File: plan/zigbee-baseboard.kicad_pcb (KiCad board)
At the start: 4 copper layers, 15.3 x 20.6 mm, 55 parts, among them J1 Debug_SWD_Pogo_2x3, J2 EFR32MG24_Core_Expansion_L12, SW1 EVPBB2A9B000, U1 EFR32MG24B020F1536IM48-B, Y1 XTL501250-S315-038

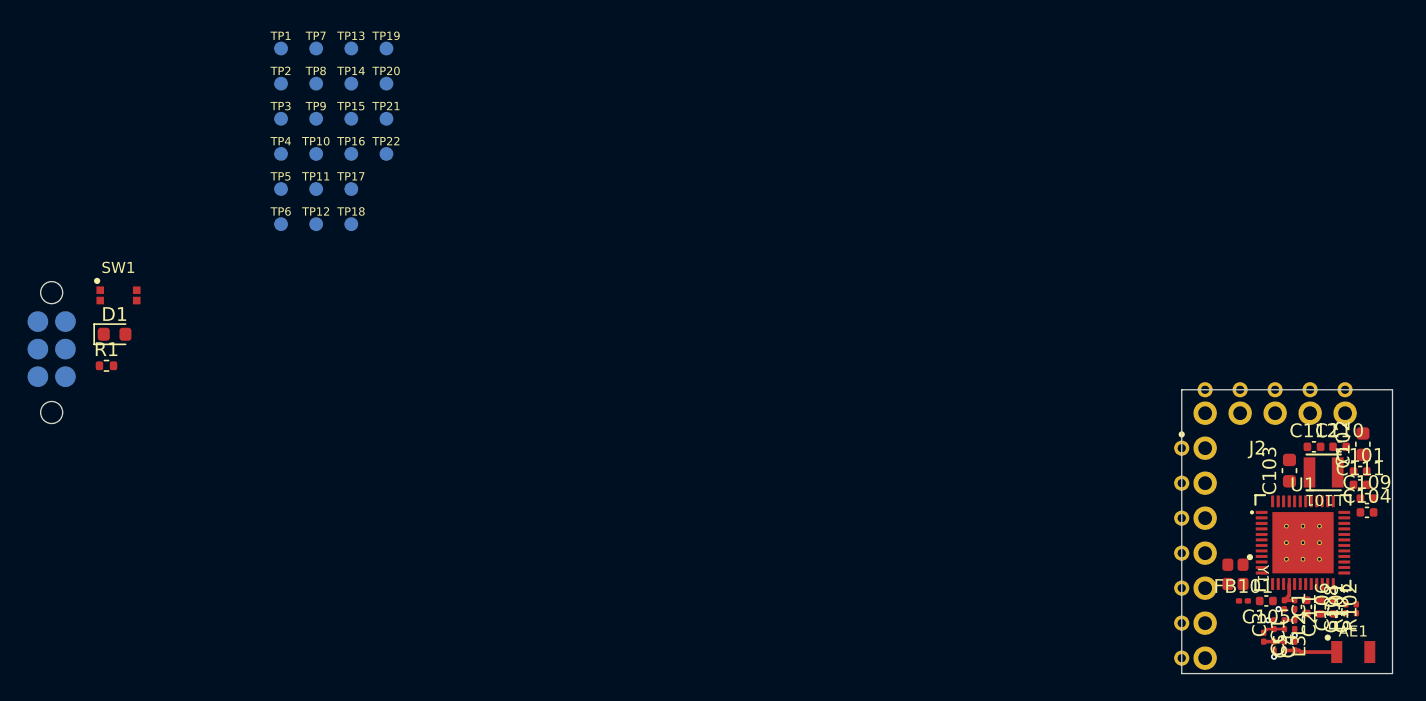
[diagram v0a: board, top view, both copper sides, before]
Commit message: Adapt and place programming/debug pad
- Remove NPTH holes because they require too much space
- Place pad on board bottom side
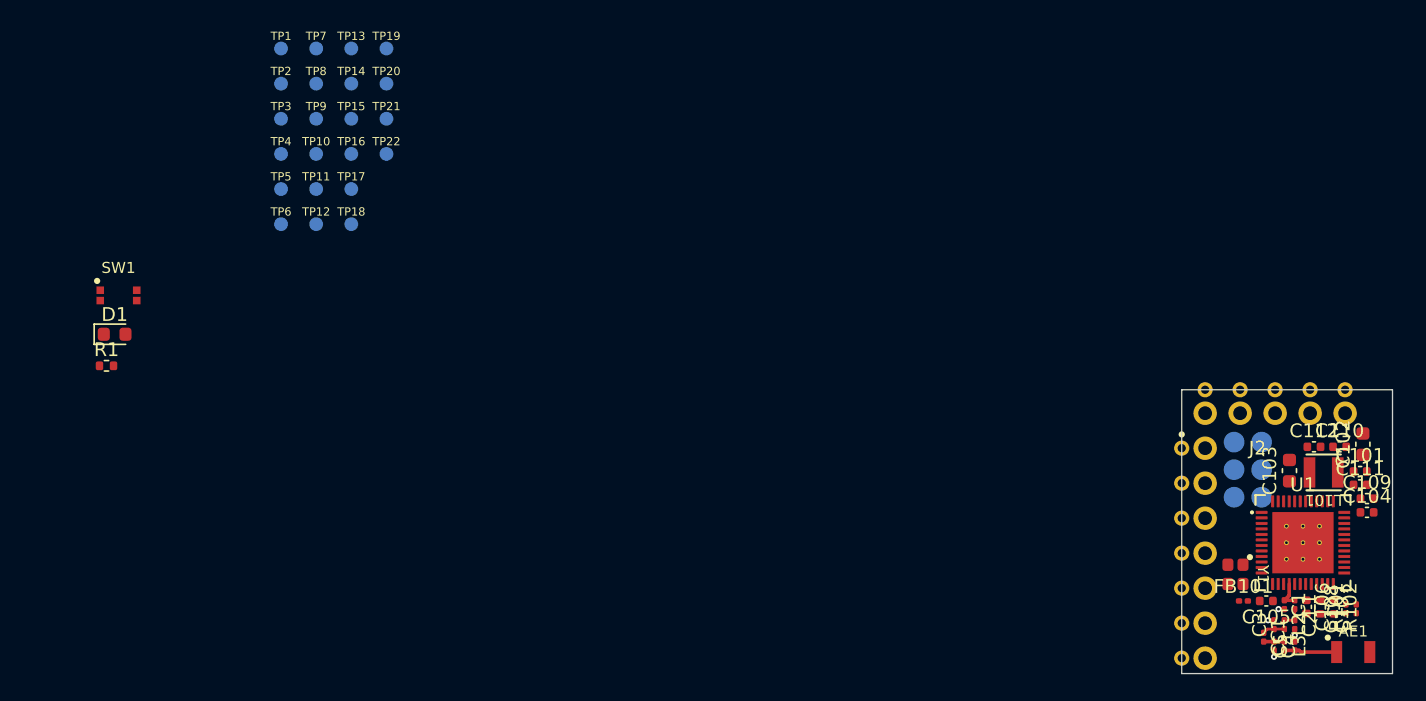
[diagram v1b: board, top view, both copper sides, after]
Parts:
- J1: value Debug_SWD_Pogo_2x3 -> Debug_SWD_Pogo_2x3_P2.00mm
- moved J1 87.3 mm to (139.0, 88.2), turned to 180 degrees
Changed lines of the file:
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@@
 		(sheetname "/Expansion/")
 		(sheetfile "Expansion.kicad_sch")
+		(units
+			(unit
+				(name "A")
+				(pins "1" "2" "3" "4" "5" "6" "7" "8" "9" "10" "11" "12")
+			)
+		)
 		(attr smd)
 		(duplicate_pad_numbers_are_jumpers no)
@@
 	)
 	(footprint "Smarthome:Debug_SWD_Pogo_2x3_P2.00mm"
+		(locked yes)
 		(layer "F.Cu")
-		(at 52.175 79.45)
+		(at 139 88.2 180)
+		(descr "6-pin 2x3 SWD pogo-pad interface, 2.00 mm pitch, bottom-side SMD contact pads, without alignment holes")
+		(tags "SWD debug pogo programming 2x3 2.00mm bottom")
 		(property "Reference" "J1"
-			(at 0 -5.8 0)
+			(at 0 -5.8 180)
 			(unlocked yes)
 			(layer "B.SilkS")
@@
 			)
 		)
-		(property "Value" "Debug_SWD_Pogo_2x3"
-			(at 0 7.5 0)
+		(property "Value" "Debug_SWD_Pogo_2x3_P2.00mm"
+			(at 0 7.5 180)
 			(unlocked yes)
 			(layer "F.Fab")
@@
 		)
 		(property "Datasheet" ""
-			(at 0 0 0)
-			(unlocked yes)
-			(layer "F.Fab")
-			(hide yes)
-			(effects
-				(font
-					(size 1 1)
-					(thickness 0.15)
-				)
-			)
-		)
-		(property "Description" "6-pin SWD programming interface with 2x3 pogo pads and two asymmetric NPTH alignment holes"
-			(at 0 0 0)
+			(at 0 0 180)
+			(unlocked yes)
+			(layer "F.Fab")
+			(hide yes)
+			(effects
+				(font
+					(size 1 1)
+					(thickness 0.15)
+				)
+			)
+		)
+		(property "Description" "6-pin SWD pogo programming interface, 2x3, 2.00 mm pitch, without alignment holes"
+			(at 0 0 180)
 			(unlocked yes)
 			(layer "F.Fab")
@@
 		(sheetname "/UserDebug/")
 		(sheetfile "UserDebug.kicad_sch")
-		(units
-			(unit
-				(name "A")
-				(pins "1" "2" "3" "4" "5" "6")
-			)
-		)
 		(attr smd)
 		(duplicate_pad_numbers_are_jumpers no)
@@
 		)
 		(fp_rect
-			(start -2 -5.15)
-			(end 2 5.65)
+			(start -2 -3)
+			(end 2 3)
 			(stroke
 				(width 0.05)
@@
 		)
 		(fp_text user "${REFERENCE}"
-			(at 0 6.3 0)
+			(at 0 6.3 180)
 			(unlocked yes)
 			(layer "B.Fab")
@@
 			)
 		)
-		(pad "" np_thru_hole circle
-			(at 0 -4.1)
-			(size 1.6 1.6)
-			(drill 1.6)
-			(layers "*.Cu" "*.Mask")
-		)
-		(pad "" np_thru_hole circle
-			(at 0 4.6)
-			(size 1.6 1.6)
-			(drill 1.6)
-			(layers "*.Cu" "*.Mask")
-		)
 		(pad "1" smd circle
-			(at -1 -2)
+			(at -1 -2 180)
 			(size 1.5 1.5)
 			(layers "B.Cu" "B.Mask")
@@
 		)
 		(pad "2" smd circle
-			(at 1 -2)
+			(at 1 -2 180)
 			(size 1.5 1.5)
 			(layers "B.Cu" "B.Mask")
@@
 		)
 		(pad "3" smd circle
-			(at -1 0)
+			(at -1 0 180)
 			(size 1.5 1.5)
 			(layers "B.Cu" "B.Mask")
@@
 		)
 		(pad "4" smd circle
-			(at 1 0)
+			(at 1 0 180)
 			(size 1.5 1.5)
 			(layers "B.Cu" "B.Mask")
@@
 		)
 		(pad "5" smd circle
-			(at -1 2)
+			(at -1 2 180)
 			(size 1.5 1.5)
 			(layers "B.Cu" "B.Mask")
@@
 		)
 		(pad "6" smd circle
-			(at 1 2)
+			(at 1 2 180)
 			(size 1.5 1.5)
 			(layers "B.Cu" "B.Mask")

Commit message: Place pairing-button
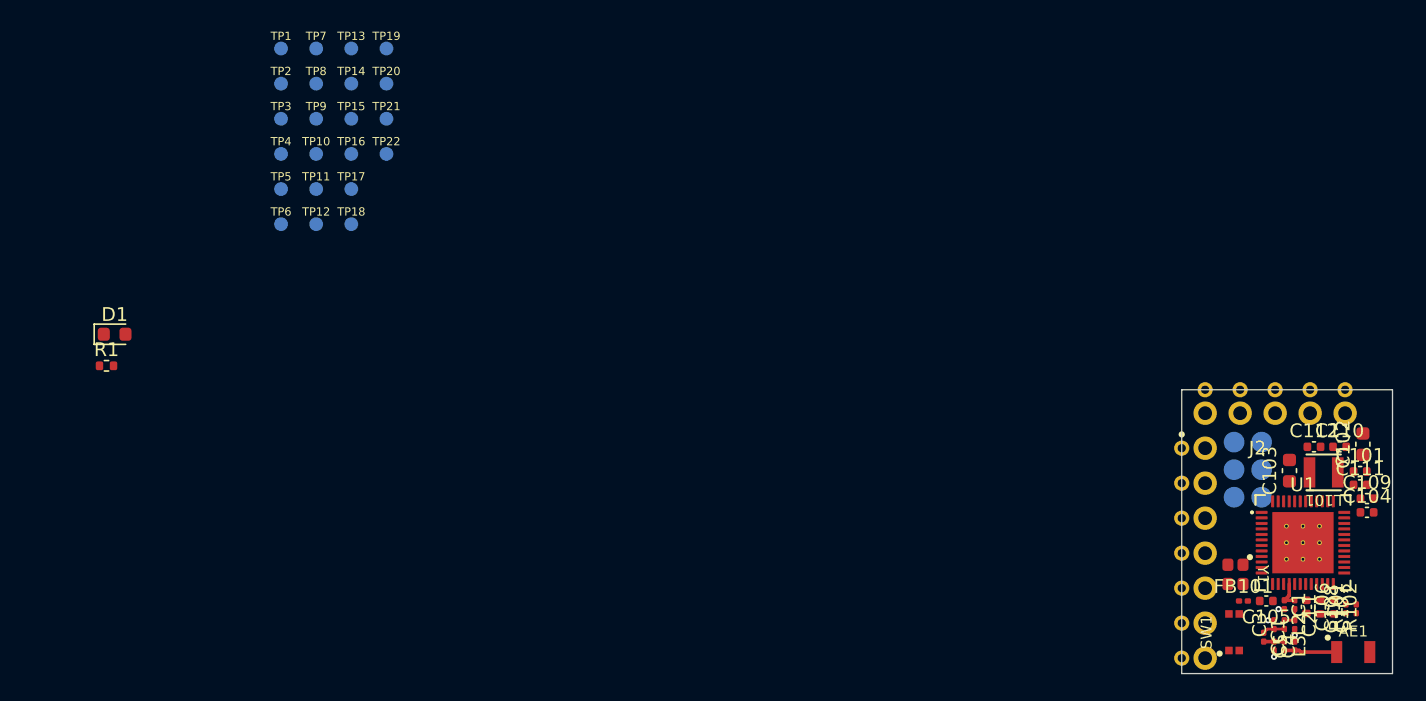
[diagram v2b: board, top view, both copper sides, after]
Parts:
- moved SW1 84.6 mm to (138.0, 100.0), turned to 90 degrees
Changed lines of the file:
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@@
 	)
 	(footprint "Smarthome:Button_Panasonic_EVPBB_2.6x1.6mm"
+		(locked yes)
 		(layer "F.Cu")
-		(at 57.025 75.55)
+		(at 138 100 90)
 		(descr "Panasonic EVP-BB series SMD light touch switch, 2.6 x 1.6 mm, top push, 4 pads")
 		(tags "Panasonic EVPBB EVP-BB tactile switch button 2.6x1.6 SMD")
 		(property "Reference" "SW1"
-			(at 0 -2 0)
+			(at 0 -2 90)
 			(unlocked yes)
 			(layer "F.SilkS")
@@
 		)
 		(property "Value" "EVPBB2A9B000"
-			(at 0 2 0)
+			(at 0 2 90)
 			(unlocked yes)
 			(layer "F.Fab")
@@
 		)
 		(property "Datasheet" "https://industrial.panasonic.com/cdbs/www-data/pdf/ATK0000/ATK0000C362.pdf"
-			(at 0 0 0)
+			(at 0 0 90)
 			(unlocked yes)
 			(layer "F.Fab")
@@
 		)
 		(property "Description" "Panasonic EVPBB2A9B000, SMD light touch switch, SPST-NO, top push, 2.6 x 1.6 x 0.53 mm, 1.6 N"
-			(at 0 0 0)
+			(at 0 0 90)
 			(unlocked yes)
 			(layer "F.Fab")
@@
 		)
 		(fp_line
+			(start 1.3 -0.8)
+			(end -1 -0.8)
+			(stroke
+				(width 0.1)
+				(type default)
+			)
+			(layer "F.Fab")
+		)
+		(fp_line
 			(start -1.3 -0.5)
 			(end -1 -0.8)
+			(stroke
+				(width 0.1)
+				(type default)
+			)
+			(layer "F.Fab")
+		)
+		(fp_line
+			(start 1.3 0.8)
+			(end 1.3 -0.8)
 			(stroke
 				(width 0.1)
@@
 			(layer "F.Fab")
 		)
-		(fp_line
-			(start 1.3 -0.8)
-			(end -1 -0.8)
-			(stroke
-				(width 0.1)
-				(type default)
-			)
-			(layer "F.Fab")
-		)
-		(fp_line
-			(start 1.3 0.8)
-			(end 1.3 -0.8)
-			(stroke
-				(width 0.1)
-				(type default)
-			)
-			(layer "F.Fab")
-		)
 		(fp_text user "${REFERENCE}"
-			(at 0 0 0)
+			(at 0 0 90)
 			(unlocked yes)
 			(layer "F.Fab")
@@
 		)
 		(pad "1" smd rect
-			(at -1.325 -0.375)
+			(at -1.325 -0.375 90)
 			(size 0.55 0.55)
 			(layers "F.Cu" "F.Mask" "F.Paste")
@@
 		)
 		(pad "1" smd rect
-			(at -1.325 0.375)
+			(at -1.325 0.375 90)
 			(size 0.55 0.55)
 			(layers "F.Cu" "F.Mask" "F.Paste")
@@
 		)
 		(pad "2" smd rect
-			(at 1.325 -0.375)
+			(at 1.325 -0.375 90)
 			(size 0.55 0.55)
 			(layers "F.Cu" "F.Mask" "F.Paste")
@@
 		)
 		(pad "2" smd rect
-			(at 1.325 0.375)
+			(at 1.325 0.375 90)
 			(size 0.55 0.55)
 			(layers "F.Cu" "F.Mask" "F.Paste")

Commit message: Place status LED
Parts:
- moved D1 83.0 mm to (138.4, 93.0), turned to -90 degrees
- moved R1 82.0 mm to (137.2, 93.0), turned to -90 degrees
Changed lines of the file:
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@@
 	)
 	(footprint "LED_SMD:LED_0603_1608Metric"
+		(locked yes)
 		(layer "F.Cu")
-		(at 56.745 78.37)
+		(at 138.4 93 -90)
 		(descr "LED SMD 0603 (1608 Metric), square (rectangular) end terminal, IPC-7351 nominal, (Body size source: http://www.tortai-tech.com/upload/download/2011102023233369053.pdf)")
 		(tags "LED")
 		(property "Reference" "D1"
-			(at 0 -1.43 0)
+			(at 0 -1.43 90)
 			(layer "F.SilkS")
 			(effects
@@
 		)
 		(property "Value" "APT1608LZGCK"
-			(at 0 1.43 0)
+			(at 0 1.43 90)
 			(layer "F.Fab")
 			(effects
@@
 		)
 		(property "Datasheet" ""
-			(at 0 0 0)
+			(at 0 0 90)
 			(layer "F.Fab")
 			(hide yes)
@@
 		)
 		(property "Description" "Light emitting diode"
-			(at 0 0 0)
+			(at 0 0 90)
 			(layer "F.Fab")
 			(hide yes)
@@
 		)
 		(property "KiLib_Generator" "SMD_2terminal_chip_molded"
-			(at 0 0 0)
+			(at 0 0 90)
 			(layer "F.SilkS")
 			(hide yes)
@@
 		)
 		(property "Sim.Pins" "1=K 2=A"
-			(at 0 0 0)
+			(at 0 0 270)
 			(unlocked yes)
 			(layer "F.Fab")
@@
 		)
 		(property "Manufacturer" "Kingbright"
-			(at 0 0 0)
+			(at 0 0 270)
 			(unlocked yes)
 			(layer "F.Fab")
@@
 		)
 		(property "Color" "green"
-			(at 0 0 0)
+			(at 0 0 270)
 			(unlocked yes)
 			(layer "F.Fab")
@@
 		)
 		(property "Package" "0603 / 1608 metric"
-			(at 0 0 0)
+			(at 0 0 270)
 			(unlocked yes)
 			(layer "F.Fab")
@@
 		(duplicate_pad_numbers_are_jumpers no)
 		(fp_line
+			(start -1.485 0.735)
+			(end 0.8 0.735)
+			(stroke
+				(width 0.12)
+				(type solid)
+			)
+			(layer "F.SilkS")
+		)
+		(fp_line
 			(start -1.485 -0.735)
 			(end -1.485 0.735)
-			(stroke
-				(width 0.12)
-				(type solid)
-			)
-			(layer "F.SilkS")
-		)
-		(fp_line
-			(start -1.485 0.735)
-			(end 0.8 0.735)
 			(stroke
 				(width 0.12)
@@
 		)
 		(fp_line
+			(start -0.8 0.4)
+			(end 0.8 0.4)
+			(stroke
+				(width 0.1)
+				(type solid)
+			)
+			(layer "F.Fab")
+		)
+		(fp_line
+			(start 0.8 0.4)
+			(end 0.8 -0.4)
+			(stroke
+				(width 0.1)
+				(type solid)
+			)
+			(layer "F.Fab")
+		)
+		(fp_line
 			(start -0.8 -0.1)
 			(end -0.8 0.4)
@@
 		)
 		(fp_line
-			(start -0.8 0.4)
-			(end 0.8 0.4)
-			(stroke
-				(width 0.1)
-				(type solid)
-			)
-			(layer "F.Fab")
-		)
-		(fp_line
 			(start -0.5 -0.4)
 			(end -0.8 -0.1)
@@
 			(layer "F.Fab")
 		)
-		(fp_line
-			(start 0.8 0.4)
-			(end 0.8 -0.4)
-			(stroke
-				(width 0.1)
-				(type solid)
-			)
-			(layer "F.Fab")
-		)
 		(fp_text user "${REFERENCE}"
-			(at 0 0 0)
+			(at 0 0 90)
 			(layer "F.Fab")
 			(effects
@@
 		)
 		(pad "1" smd roundrect
-			(at -0.7875 0)
+			(at -0.7875 0 270)
 			(size 0.875 0.95)
 			(layers "F.Cu" "F.Mask" "F.Paste")
@@
 		)
 		(pad "2" smd roundrect
-			(at 0.7875 0)
+			(at 0.7875 0 270)
 			(size 0.875 0.95)
 			(layers "F.Cu" "F.Mask" "F.Paste")
@@
 	)
 	(footprint "Resistor_SMD:R_0402_1005Metric"
+		(locked yes)
 		(layer "F.Cu")
-		(at 56.155 80.66)
+		(at 137.2 93 -90)
 		(descr "Resistor SMD 0402 (1005 Metric), square (rectangular) end terminal, IPC-7351 nominal, (Body size source: IPC-SM-782 page 72, https://www.pcb-3d.com/wordpress/wp-content/uploads/ipc-sm-782a_amendment_1_and_2.pdf)")
 		(tags "resistor")
 		(property "Reference" "R1"
-			(at 0 -1.17 0)
+			(at 0 -1.17 90)
 			(layer "F.SilkS")
 			(effects
@@
 		)
 		(property "Value" "2.2 kΩ, 1%"
-			(at 0 1.17 0)
+			(at 0 1.17 90)
 			(layer "F.Fab")
 			(effects
@@
 		)
 		(property "Datasheet" ""
-			(at 0 0 0)
+			(at 0 0 90)
 			(layer "F.Fab")
 			(hide yes)
@@
 		)
 		(property "Description" "Resistor"
-			(at 0 0 0)
+			(at 0 0 90)
 			(layer "F.Fab")
 			(hide yes)
@@
 		)
 		(property "KiLib_Generator" "SMD_2terminal_chip_molded"
-			(at 0 0 0)
+			(at 0 0 90)
 			(layer "F.SilkS")
 			(hide yes)
@@
 		(duplicate_pad_numbers_are_jumpers no)
 		(fp_line
+			(start -0.153641 0.38)
+			(end 0.153641 0.38)
+			(stroke
+				(width 0.12)
+				(type solid)
+			)
+			(layer "F.SilkS")
+		)
+		(fp_line
 			(start -0.153641 -0.38)
 			(end 0.153641 -0.38)
-			(stroke
-				(width 0.12)
-				(type solid)
-			)
-			(layer "F.SilkS")
-		)
-		(fp_line
-			(start -0.153641 0.38)
-			(end 0.153641 0.38)
 			(stroke
 				(width 0.12)
@@
 		)
 		(fp_text user "${REFERENCE}"
-			(at 0 0 0)
+			(at 0 0 90)
 			(layer "F.Fab")
 			(effects
@@
 		)
 		(pad "1" smd roundrect
-			(at -0.51 0)
+			(at -0.51 0 270)
 			(size 0.54 0.64)
 			(layers "F.Cu" "F.Mask" "F.Paste")
@@
 		)
 		(pad "2" smd roundrect
-			(at 0.51 0)
+			(at 0.51 0 270)
 			(size 0.54 0.64)
 			(layers "F.Cu" "F.Mask" "F.Paste")
